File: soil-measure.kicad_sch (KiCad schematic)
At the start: 39 parts, among them J5 USB_C_Receptacle_USB2.0_14P, J6 DE9_Socket_MountingHoles, J7 Conn_01x16, SW1 SW_SPST, U1 STM32G431CBUx, U2 TPS62130, U4 W25Q128JVP, U6 ISL3172E, Y1 8MHz

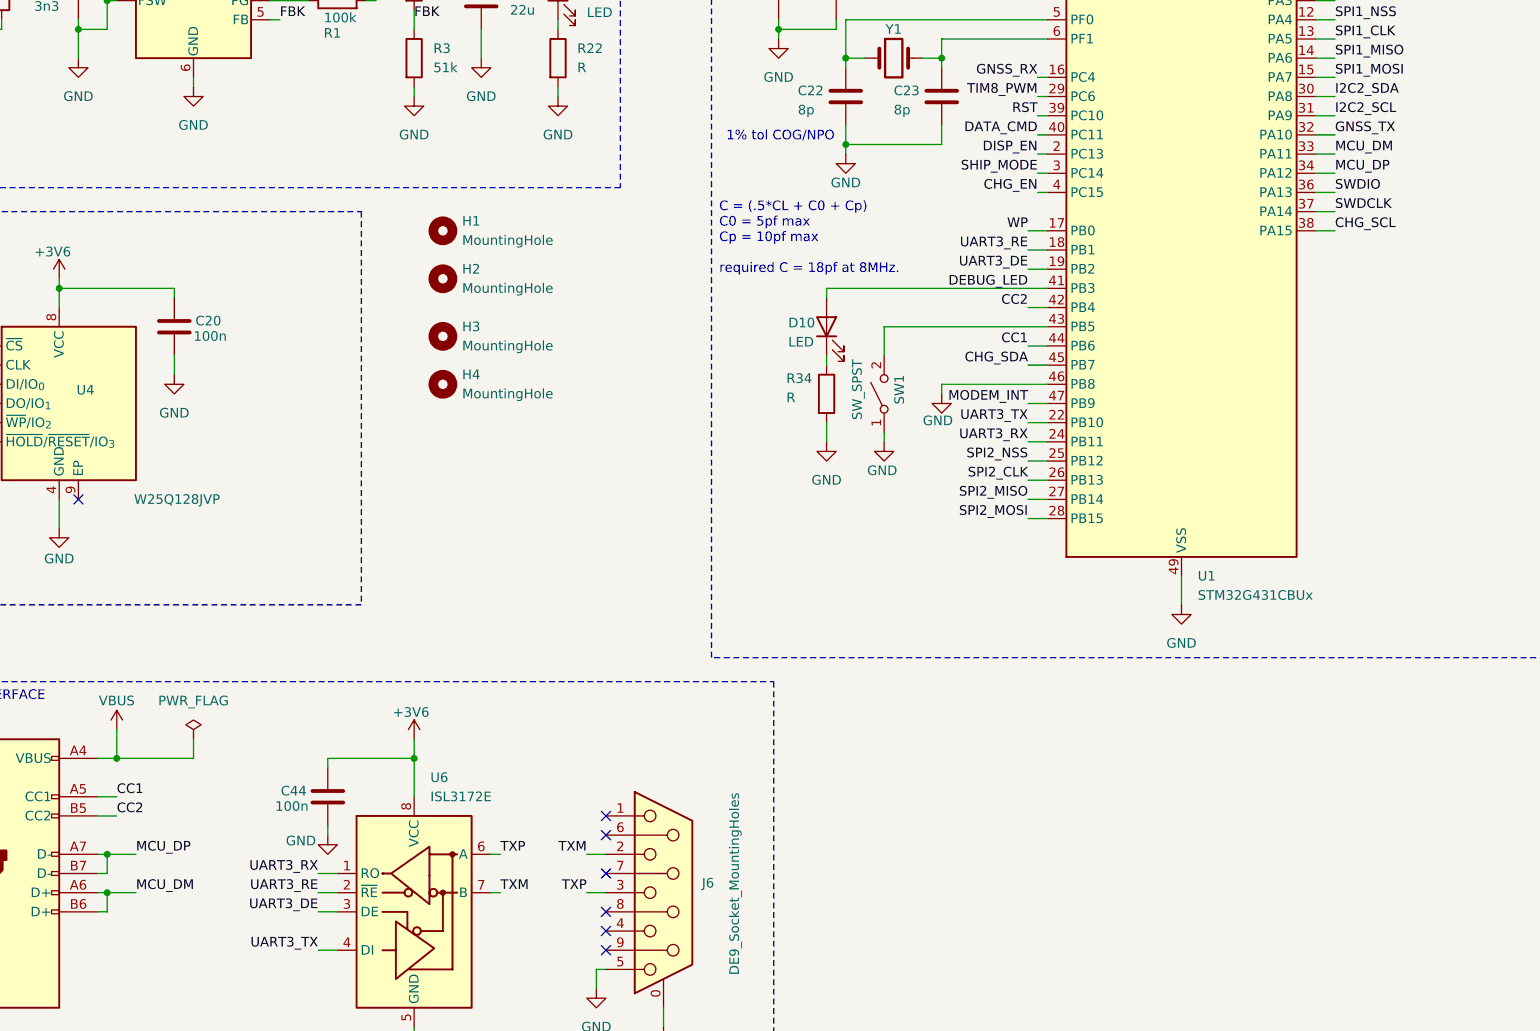
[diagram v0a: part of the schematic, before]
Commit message: Fixed bug on schematic
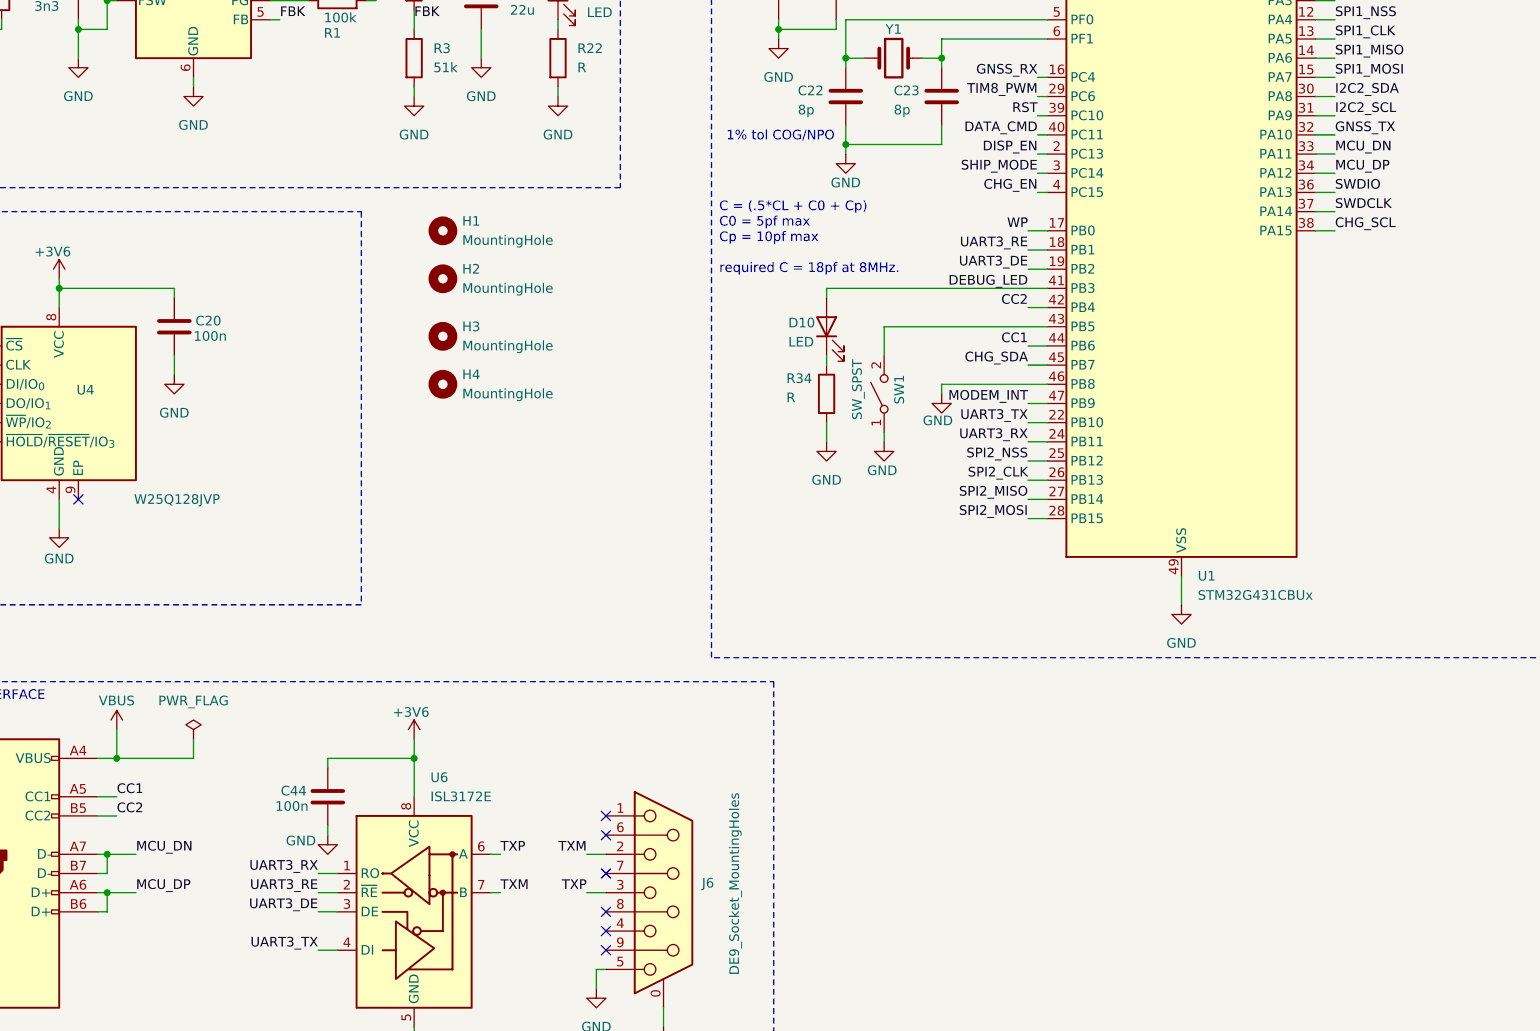
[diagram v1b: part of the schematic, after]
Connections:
- net MCU_DP: now also J5.A6 (D+), J5.B6 (D+); no longer J5.A7 (D-), J5.B7 (D-)
- removed net MCU_DM: J5.A6 (D+), J5.B6 (D+), U1.33 (PA11)
- new net MCU_DN: J5.A7 (D-), J5.B7 (D-), U1.33 (PA11)
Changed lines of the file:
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@@
 		)
 	)
-	(label "MCU_DM"
+	(label "MCU_DP"
 		(at 50.8 165.1 0)
 		(effects
@@
 		)
 	)
-	(label "MCU_DP"
+	(label "MCU_DN"
 		(at 50.8 160.02 0)
 		(effects
@@
 		)
 	)
-	(label "MCU_DM"
+	(label "MCU_DN"
 		(at 209.55 67.31 0)
 		(effects
